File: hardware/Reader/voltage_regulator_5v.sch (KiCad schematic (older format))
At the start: 5 parts

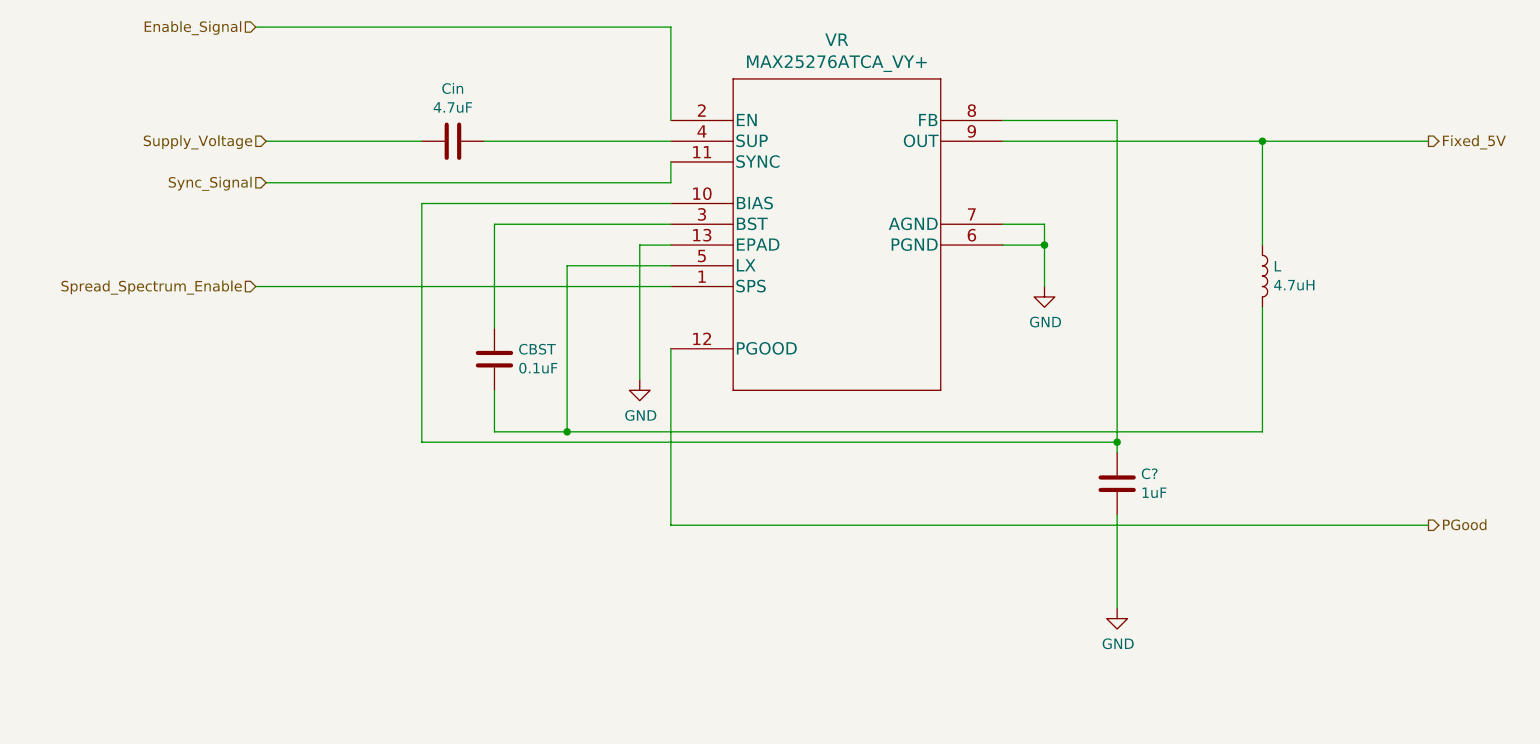
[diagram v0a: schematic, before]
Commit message: Completed schematics for reader
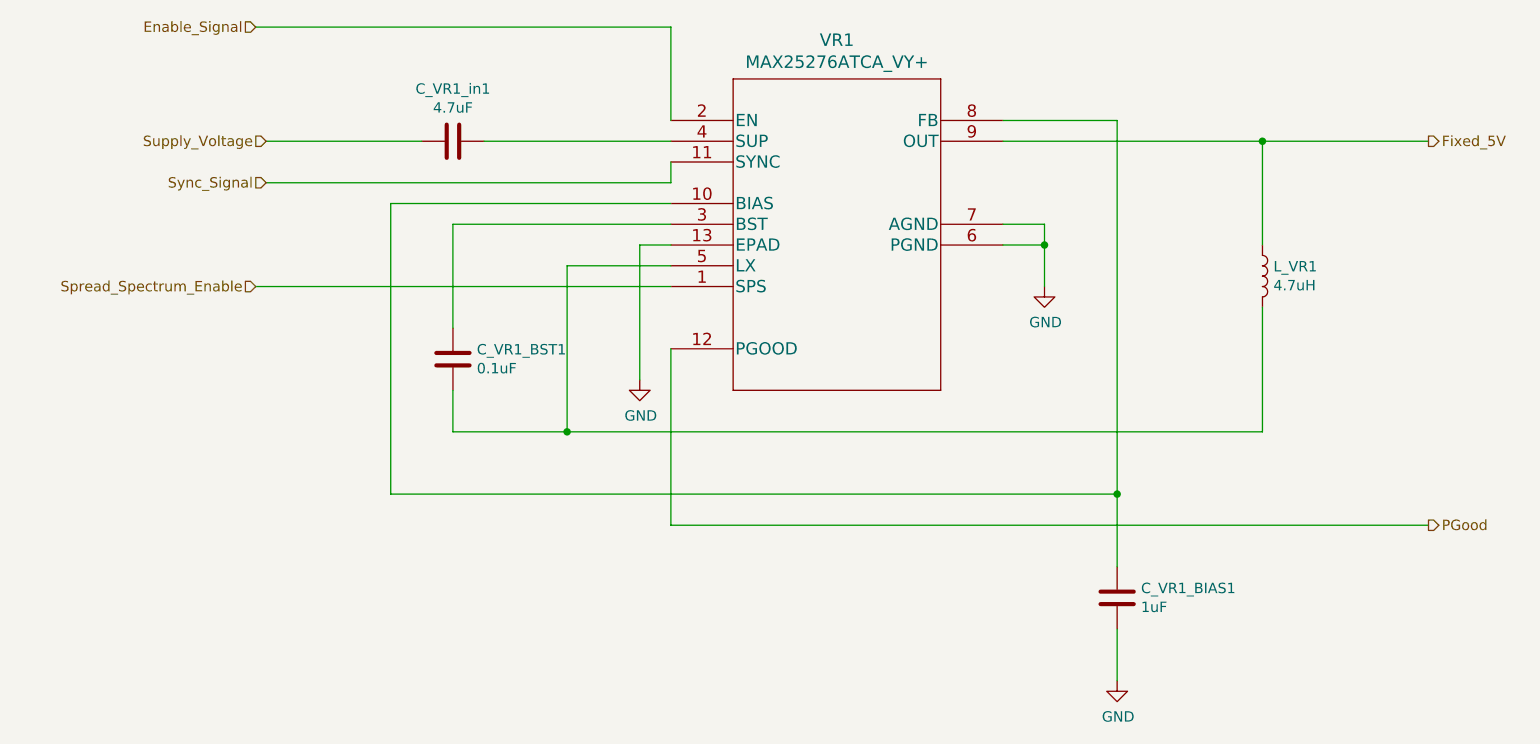
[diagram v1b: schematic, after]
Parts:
- C_VR1_BIAS1: renamed from C?; footprint (none) -> footprints:0603
- C_VR1_BST1: renamed from CBST; footprint (none) -> footprints:CAPC1608X90
- C_VR1_in1: renamed from Cin; footprint (none) -> footprints:C1206C475K3RACAUTO; Part Name (none) -> C1206C475K3RACAUTO
- L_VR1: renamed from L; footprint (none) -> footprints:CV201210-4R7K
- VR1: renamed from VR; footprint 21-100284A_TD1233Y+3C_MXM -> footprints:MAX25276ATCA&slash_VY&plus_
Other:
- moved on the sheet: C_VR1_BIAS1, C_VR1_BST1
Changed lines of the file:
@@
 EELAYER 30 0
 EELAYER END
-$Descr A4 11693 8268
+$Descr USLetter 11000 8500
 encoding utf-8
-Sheet 6 9
-Title ""
-Date ""
-Rev ""
-Comp ""
-Comment1 ""
+Sheet 3 17
+Title "CANnect Reader | Voltage Regulator (5V)"
+Date "2020-10-20"
+Rev "0.0.1"
+Comp "CANtech"
+Comment1 "Created by Choong Jin Ng | jin8383@gmail.com"
 Comment2 ""
 Comment3 ""
-Comment4 ""
+Comment4 "Component Identifier: VR1"
 $EndDescr
 $Comp
-L MAX25276ATCAVY:MAX25276ATCA_VY+ VR
+L MAX25276ATCAVY:MAX25276ATCA_VY+ VR1
 U 1 1 5F9ECE66
 P 3800 2200
-F 0 "VR" H 4600 2587 60  0000 C CNN
+F 0 "VR1" H 4600 2587 60  0000 C CNN
 F 1 "MAX25276ATCA_VY+" H 4600 2481 60  0000 C CNN
-F 2 "21-100284A_TD1233Y+3C_MXM" H 4600 2440 60  0001 C CNN
+F 2 "footprints:MAX25276ATCA&slash_VY&plus_" H 4600 2440 60  0001 C CNN
 F 3 "" H 3800 2200 60  0000 C CNN
 	1    3800 2200
@@
 L power:GND #PWR0119
 U 1 1 5F9EE8B3
-P 5950 4550
-F 0 "#PWR0119" H 5950 4300 50  0001 C CNN
-F 1 "GND" H 5955 4377 50  0000 C CNN
-F 2 "" H 5950 4550 50  0001 C CNN
-F 3 "" H 5950 4550 50  0001 C CNN
-	1    5950 4550
+P 5950 4900
+F 0 "#PWR0119" H 5950 4650 50  0001 C CNN
+F 1 "GND" H 5955 4727 50  0000 C CNN
+F 2 "" H 5950 4900 50  0001 C CNN
+F 3 "" H 5950 4900 50  0001 C CNN
+	1    5950 4900
 	1    0    0    -1
 $EndComp
@@
 	5400 2200 5950 2200
 Wire Wire Line
-	5950 2200 5950 3750
-Wire Wire Line
-	5950 4100 5950 4550
-Connection ~ 5950 3750
-Wire Wire Line
-	5950 3750 5950 3800
+	5950 4650 5950 4900
 $Comp
-L Device:C Cin
+L Device:C C_VR1_in1
 U 1 1 5F9F0C9F
 P 2750 2300
-F 0 "Cin" V 2498 2300 50  0000 C CNN
+F 0 "C_VR1_in1" V 2498 2300 50  0000 C CNN
 F 1 "4.7uF" V 2589 2300 50  0000 C CNN
-F 2 "" H 2788 2150 50  0001 C CNN
-F 3 "~" H 2750 2300 50  0001 C CNN
+F 2 "footprints:C1206C475K3RACAUTO" H 2788 2150 50  0001 C CNN
+F 3 "https://api.kemet.com/component-edge/download/specsheet/C1206C475K3RACAUTO.pdf" H 2750 2300 50  0001 C CNN
+F 4 "C1206C475K3RACAUTO" H 2750 2300 50  0001 C CNN "Part Name"
 	1    2750 2300
 	0    1    1    0
@@
 	3800 4150 7450 4150
 $Comp
-L Device:L L
+L Device:L L_VR1
 U 1 1 5F9F2ADC
 P 6650 2950
-F 0 "L" H 6703 2996 50  0000 L CNN
+F 0 "L_VR1" H 6703 2996 50  0000 L CNN
 F 1 "4.7uH" H 6703 2905 50  0000 L CNN
-F 2 "" H 6650 2950 50  0001 C CNN
-F 3 "~" H 6650 2950 50  0001 C CNN
+F 2 "footprints:CV201210-4R7K" H 6650 2950 50  0001 C CNN
+F 3 "https://www.bourns.com/docs/Product-Datasheets/CV201210.pdf" H 6650 2950 50  0001 C CNN
 	1    6650 2950
 	1    0    0    -1
@@
 	6650 2300 7450 2300
 $Comp
-L Device:C CBST
+L Device:C C_VR1_BST1
 U 1 1 5F9F38FF
-P 2950 3350
-F 0 "CBST" H 3065 3396 50  0000 L CNN
-F 1 "0.1uF" H 3065 3305 50  0000 L CNN
-F 2 "" H 2988 3200 50  0001 C CNN
-F 3 "~" H 2950 3350 50  0001 C CNN
-	1    2950 3350
+P 2750 3350
+F 0 "C_VR1_BST1" H 2865 3396 50  0000 L CNN
+F 1 "0.1uF" H 2865 3305 50  0000 L CNN
+F 2 "footprints:CAPC1608X90" H 2788 3200 50  0001 C CNN
+F 3 "https://www.yageo.com/upload/media/product/productsearch/datasheet/mlcc/UPY-GPHC_X7R_6.3V-to-50V_18.pdf" H 2750 3350 50  0001 C CNN
+	1    2750 3350
 	1    0    0    -1
 $EndComp
@@
 $EndComp
 Wire Wire Line
-	2600 2600 2600 3750
-Wire Wire Line
-	2600 2600 3800 2600
-Wire Wire Line
-	2600 3750 5950 3750
+	2450 2600 3800 2600
 Wire Wire Line
 	3650 3450 3650 2800
@@
 	3650 2800 3800 2800
 Wire Wire Line
-	3800 2700 2950 2700
+	3800 2700 2750 2700
 Wire Wire Line
-	2950 2700 2950 3200
+	2750 2700 2750 3200
 Wire Wire Line
-	2950 3500 2950 3700
+	2750 3500 2750 3700
 Wire Wire Line
-	2950 3700 3300 3700
+	2750 3700 3300 3700
 Wire Wire Line
 	6650 3700 6650 3100
@@
 	1800 3000 3800 3000
 $Comp
-L Device:C C?
+L Device:C C_VR1_BIAS1
 U 1 1 5F9EFBD6
-P 5950 3950
-F 0 "C?" H 6065 3996 50  0000 L CNN
-F 1 "1uF" H 6065 3905 50  0000 L CNN
-F 2 "" H 5988 3800 50  0001 C CNN
-F 3 "~" H 5950 3950 50  0001 C CNN
-	1    5950 3950
+P 5950 4500
+F 0 "C_VR1_BIAS1" H 6065 4546 50  0000 L CNN
+F 1 "1uF" H 6065 4455 50  0000 L CNN
+F 2 "footprints:0603" H 5988 4350 50  0001 C CNN
+F 3 "https://content.kemet.com/datasheets/KEM_C1002_X7R_SMD.pdf" H 5950 4500 50  0001 C CNN
+	1    5950 4500
 	1    0    0    -1
 $EndComp
+Wire Wire Line
+	5950 2200 5950 4000
+Wire Wire Line
+	2450 4000 5950 4000
+Wire Wire Line
+	2450 2600 2450 4000
+Connection ~ 5950 4000
+Wire Wire Line
+	5950 4000 5950 4350
 $EndSCHEMATC

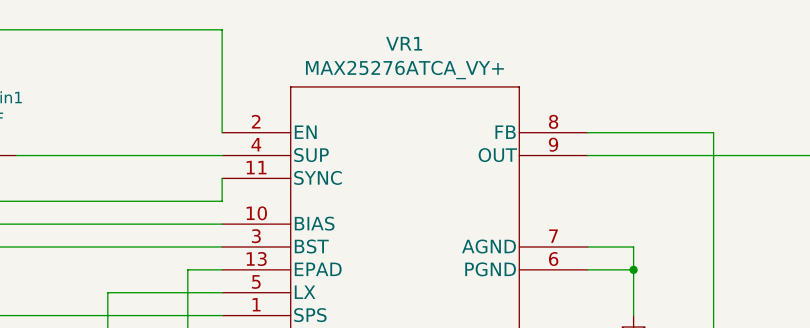
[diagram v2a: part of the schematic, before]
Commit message: Added ESD Protection. Fixed minor bugs on schematic. Attempted placement of components
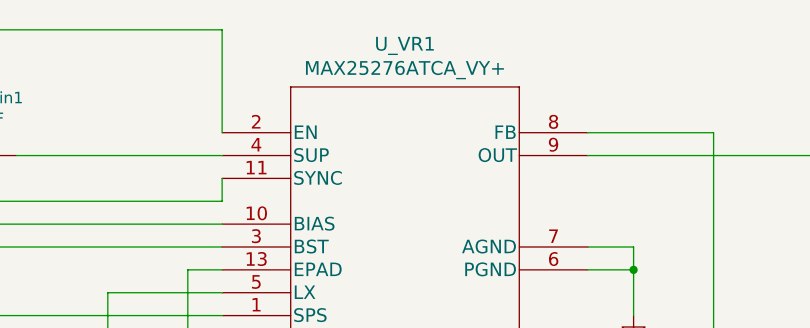
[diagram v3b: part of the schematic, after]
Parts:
- renumbered VR1 to U_VR1
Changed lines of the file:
@@
 $Descr USLetter 11000 8500
 encoding utf-8
-Sheet 3 18
+Sheet 18 19
 Title "CANnect Reader | Voltage Regulator (5V)"
-Date "2020-10-20"
-Rev "0.0.01"
+Date "2020-10-25"
+Rev "0.0.03"
 Comp "CANtech"
 Comment1 "Created by Choong Jin Ng | jin8383@gmail.com"
@@
 $EndDescr
 $Comp
-L MAX25276ATCAVY:MAX25276ATCA_VY+ VR1
+L MAX25276ATCAVY:MAX25276ATCA_VY+ U_VR1
 U 1 1 5F9ECE66
 P 3800 2200
-F 0 "VR1" H 4600 2587 60  0000 C CNN
+F 0 "U_VR1" H 4600 2587 60  0000 C CNN
 F 1 "MAX25276ATCA_VY+" H 4600 2481 60  0000 C CNN
 F 2 "footprints:MAX25276ATCA&slash_VY&plus_" H 4600 2440 60  0001 C CNN

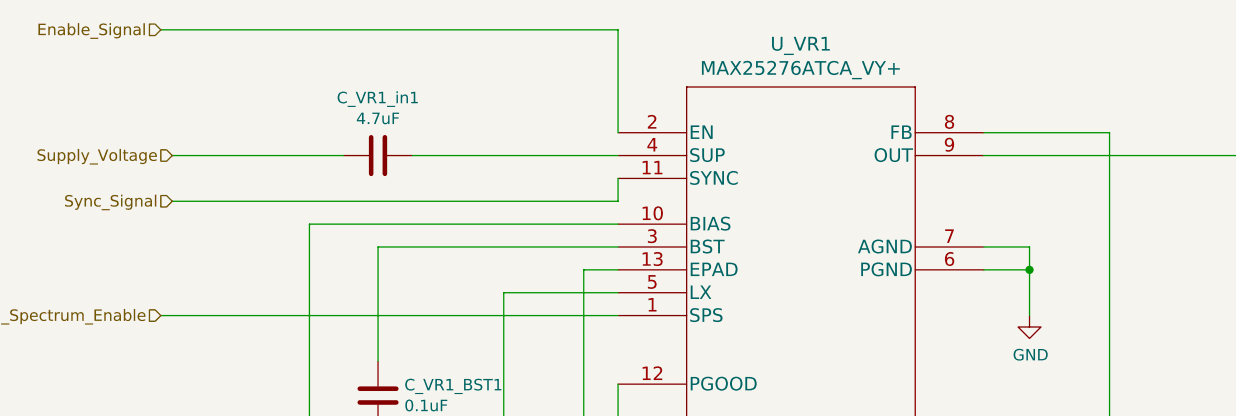
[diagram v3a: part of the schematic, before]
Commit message: Fixed bugs on the reader schematic. Exported Schematic Electrical report
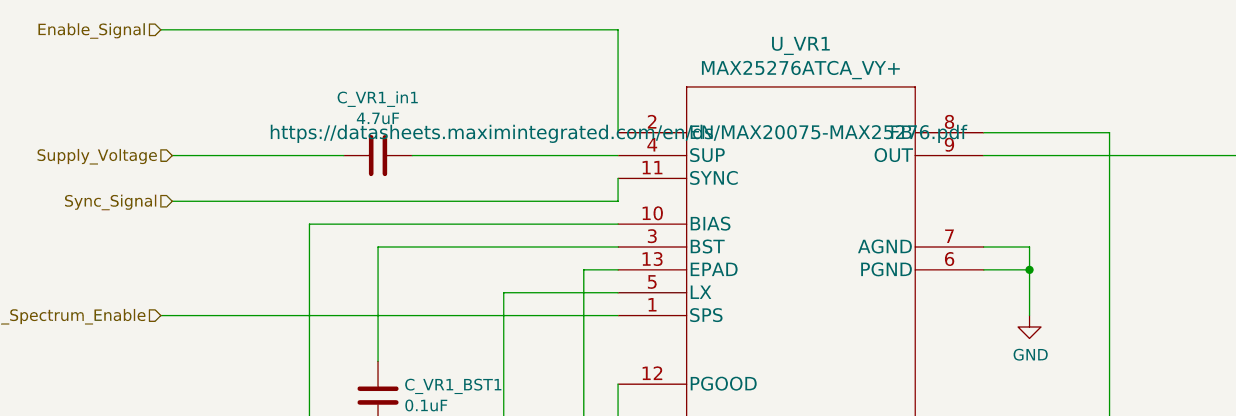
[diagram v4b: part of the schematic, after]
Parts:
- C_VR1_BIAS1: Manufacturer (none) -> Kermet; Part Name (none) -> C0603C105K4RACTU; Vendor (none) -> DigiKey Canada; digikeypn (none) -> 399-7847-1-ND
- C_VR1_BST1: Manufacturer (none) -> Yageo; Part Name (none) -> CC0603JRX7R8BB104; Vendor (none) -> DigiKey Canada; digikeypn (none) -> 311-1777-1-ND
- C_VR1_in1: Manufacturer (none) -> Kermet; Vendor (none) -> DigiKey Canada; digikeypn (none) -> 399-7029-1-ND
- L_VR1: Manufacturer (none) -> Bourns Inc.; Part Name (none) -> CV201210-4R7K; Vendor (none) -> DigiKey Canada; digikeypn (none) -> CV201210-4R7KCT-ND
- U_VR1: Manufacturer (none) -> Maxim Integrated; Part Name (none) -> MAX25276ATCA/VY+; Vendor (none) -> DigiKey Canada; digikeypn (none) -> 175-MAX25276ATCA/VY+-ND
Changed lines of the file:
@@
 F 1 "MAX25276ATCA_VY+" H 4600 2481 60  0000 C CNN
 F 2 "footprints:MAX25276ATCA&slash_VY&plus_" H 4600 2440 60  0001 C CNN
-F 3 "" H 3800 2200 60  0000 C CNN
+F 3 "https://datasheets.maximintegrated.com/en/ds/MAX20075-MAX25276.pdf" H 3800 2200 60  0000 C CNN
+F 4 "MAX25276ATCA/VY+" H 3800 2200 50  0001 C CNN "Part Name"
+F 5 "Maxim Integrated" H 3800 2200 50  0001 C CNN "Manufacturer"
+F 6 "DigiKey Canada" H 3800 2200 50  0001 C CNN "Vendor"
+F 7 "175-MAX25276ATCA/VY+-ND" H 3800 2200 50  0001 C CNN "digikeypn"
 	1    3800 2200
 	1    0    0    -1
@@
 F 3 "https://api.kemet.com/component-edge/download/specsheet/C1206C475K3RACAUTO.pdf" H 2750 2300 50  0001 C CNN
 F 4 "C1206C475K3RACAUTO" H 2750 2300 50  0001 C CNN "Part Name"
+F 5 "Kermet" H 2750 2300 50  0001 C CNN "Manufacturer"
+F 6 "DigiKey Canada" H 2750 2300 50  0001 C CNN "Vendor"
+F 7 "399-7029-1-ND" H 2750 2300 50  0001 C CNN "digikeypn"
 	1    2750 2300
 	0    1    1    0
@@
 F 2 "footprints:CV201210-4R7K" H 6650 2950 50  0001 C CNN
 F 3 "https://www.bourns.com/docs/Product-Datasheets/CV201210.pdf" H 6650 2950 50  0001 C CNN
+F 4 "CV201210-4R7K" H 6650 2950 50  0001 C CNN "Part Name"
+F 5 "DigiKey Canada" H 6650 2950 50  0001 C CNN "Vendor"
+F 6 "Bourns Inc." H 6650 2950 50  0001 C CNN "Manufacturer"
+F 7 "CV201210-4R7KCT-ND" H 6650 2950 50  0001 C CNN "digikeypn"
 	1    6650 2950
 	1    0    0    -1
@@
 F 2 "footprints:CAPC1608X90" H 2788 3200 50  0001 C CNN
 F 3 "https://www.yageo.com/upload/media/product/productsearch/datasheet/mlcc/UPY-GPHC_X7R_6.3V-to-50V_18.pdf" H 2750 3350 50  0001 C CNN
+F 4 "CC0603JRX7R8BB104" H 2750 3350 50  0001 C CNN "Part Name"
+F 5 "Yageo" H 2750 3350 50  0001 C CNN "Manufacturer"
+F 6 "DigiKey Canada" H 2750 3350 50  0001 C CNN "Vendor"
+F 7 "311-1777-1-ND" H 2750 3350 50  0001 C CNN "digikeypn"
 	1    2750 3350
 	1    0    0    -1
@@
 F 2 "footprints:0603" H 5988 4350 50  0001 C CNN
 F 3 "https://content.kemet.com/datasheets/KEM_C1002_X7R_SMD.pdf" H 5950 4500 50  0001 C CNN
+F 4 "C0603C105K4RACTU" H 5950 4500 50  0001 C CNN "Part Name"
+F 5 "Kermet" H 5950 4500 50  0001 C CNN "Manufacturer"
+F 6 "DigiKey Canada" H 5950 4500 50  0001 C CNN "Vendor"
+F 7 "399-7847-1-ND" H 5950 4500 50  0001 C CNN "digikeypn"
 	1    5950 4500
 	1    0    0    -1
